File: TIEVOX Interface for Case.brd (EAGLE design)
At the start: 92.5 x 80 mm, 22 parts, among them U4 CAT24C32.UDFN8

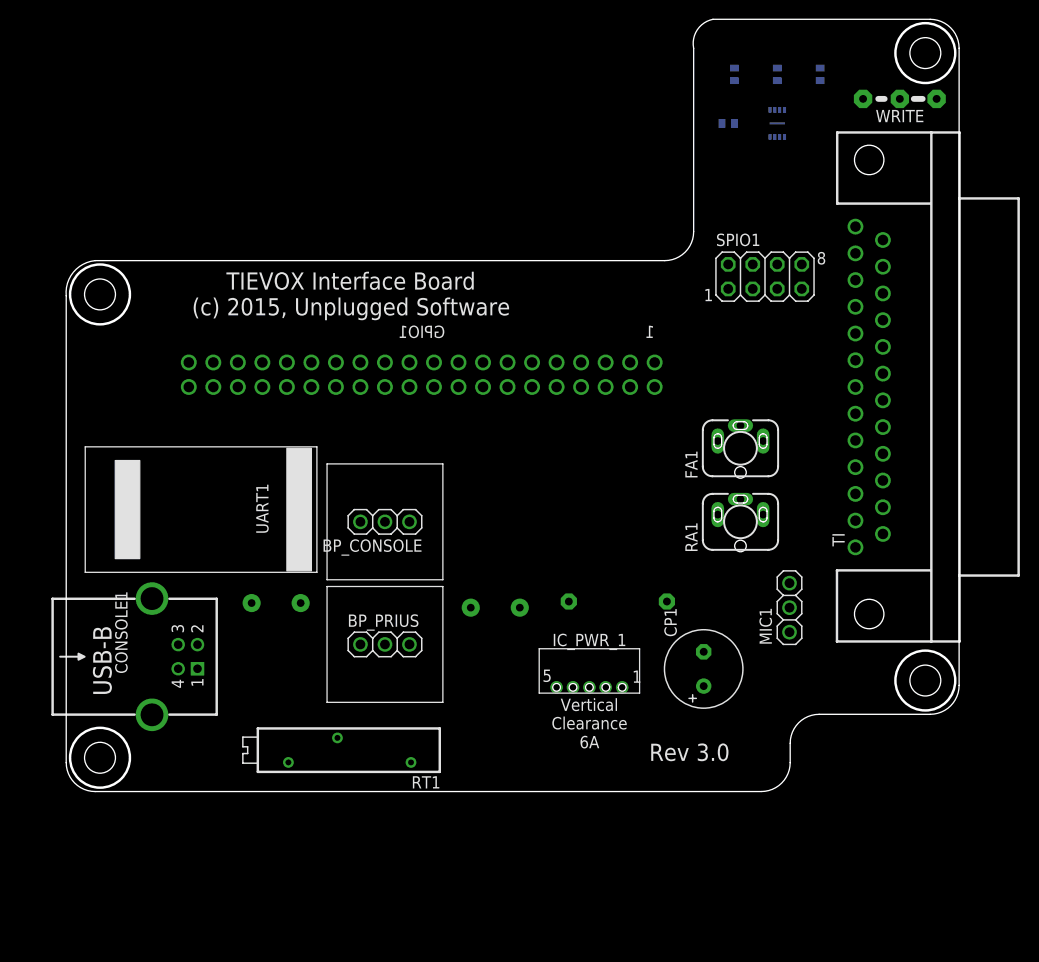
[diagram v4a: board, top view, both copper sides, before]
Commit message: Another attempt to build Interface without vias.
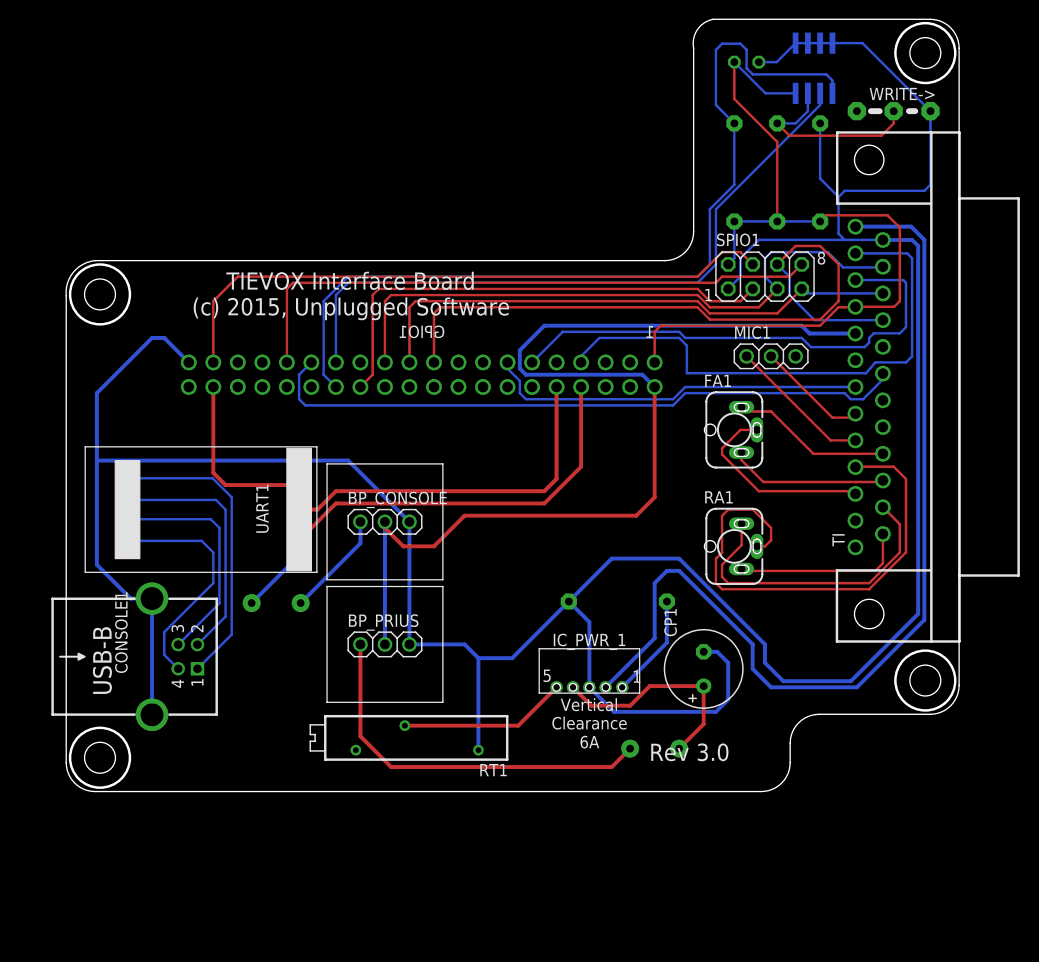
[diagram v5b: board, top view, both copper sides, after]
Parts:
- removed WRITE: (no value), jumper:04C
- added WRITE->: (no value), jumper:04C
- C1: device adafruit:C1005 -> adafruit:C025-050X050
- R6, R7, R8: device adafruit:R1005 -> adafruit:0207/10
- U4: device on-semiconductor:UDFN8 -> microbuilder:SOIC8_150MIL
- moved MIC1 26.1 mm to (73.0, 45.1), turned to 0 degrees
- moved F1 22.0 mm to (61.0, 4.45), turned to 0 degrees
- moved R6 10.2 mm to (73.7, 64.1), turned to 270 degrees
- moved R7 10.2 mm to (69.2, 64.1), turned to 270 degrees
- moved R8 10.2 mm to (78.1, 64.1), turned to 270 degrees
- moved RT1 7.10 mm to (35.1, 5.56)
- moved U4 6.87 mm to (77.5, 74.9)
- moved C1 6.63 mm to (70.5, 75.6), turned to 0 degrees
- moved RA1 2.62 mm to (69.2, 25.4), turned to 270 degrees
- moved FA1 2.01 mm to (69.2, 37.5), turned to 270 degrees
- turned BP_CONSOLE to 0 degrees
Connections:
- removed net 39_GND: GPIO1.39_GND
- new net 14_GND: GPIO1.14_GND
- new net 6_GND: GPIO1.6_GND
- net GND: now also GPIO1.39_GND, WRITE->.3; no longer GPIO1.14_GND, GPIO1.6_GND, U4.PAD, WRITE.3
- net N$39: now also WRITE->.2; no longer WRITE.2
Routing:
- net GND: track 0.00 -> 320.1 mm
- net +5VDC: track 0.00 -> 108.4 mm
- net PWR12_IN: track 0.00 -> 97.8 mm
- net N$40: track 0.00 -> 91.4 mm
- net +3.3VDC: track 0.00 -> 86.2 mm
- net N$1: track 0.00 -> 74.8 mm
- net N$38: track 0.00 -> 69.9 mm
- net N$11: track 0.00 -> 67.3 mm
- net N$3: track 0.00 -> 65.4 mm
- net N$6: track 0.00 -> 64.9 mm
- net N$5: track 0.00 -> 62.0 mm
- net N$2: track 0.00 -> 56.8 mm
- net N$7: track 0.00 -> 55.9 mm
- net N$8: track 0.00 -> 51.8 mm
- net N$21: track 0.00 -> 51.3 mm
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
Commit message: Updated TIEVOX Interface for Case:
- Removed console circuit
- Replaced audio jacks to use ones purchased
- Remapped circuit schematic
- Added backpower protection back in
- Still needs traces drawn.
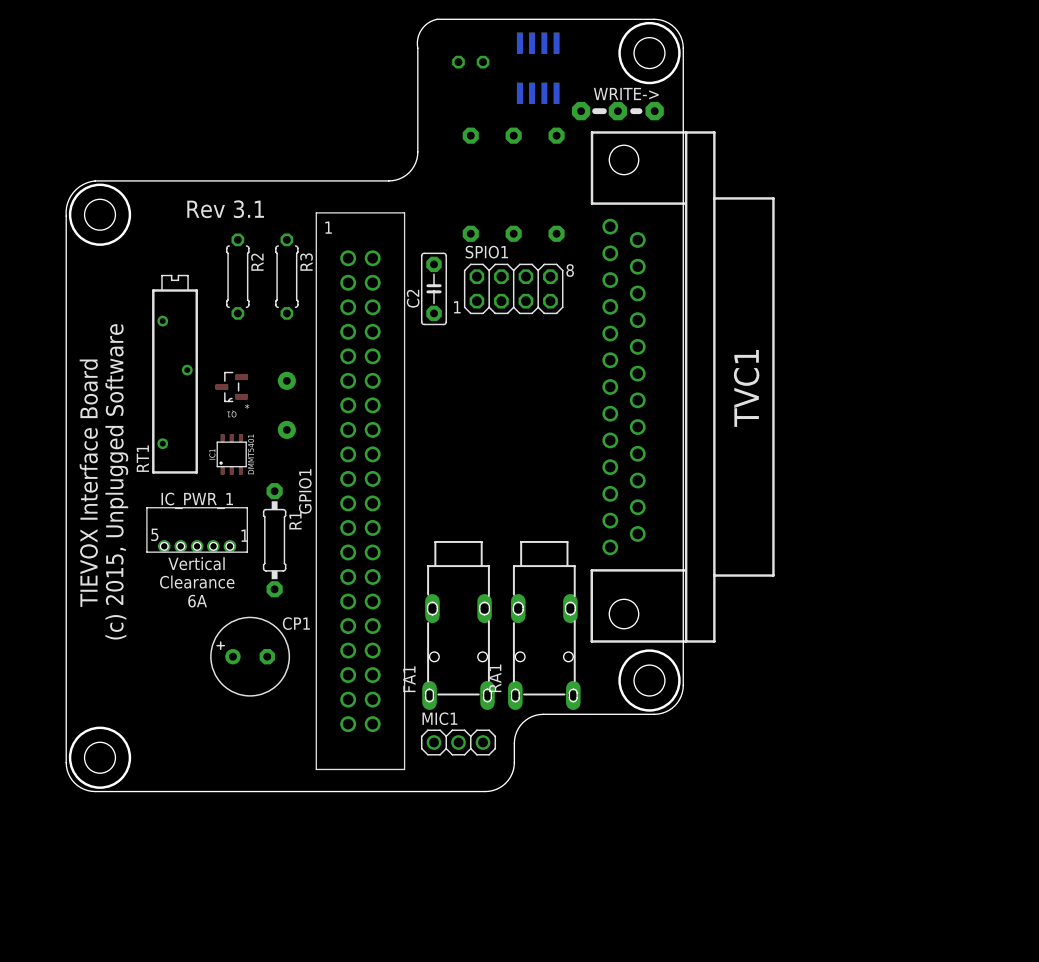
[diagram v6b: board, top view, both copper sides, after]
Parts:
- removed BP_CONSOLE, BP_PRIUS: BACKPOWER, connectors:BACKPOWER
- removed CONSOLE1: (no value), connector:USBBF-1
- removed F2: 06R155BPR, SparkFun-PowerIC:PTC
- removed TI: D-SUB25-H5R25RA, con-thomas-betts:H5R25RA
- removed UART1: GS27159, packages:GS27159
- added C2: 0.1uf, capacitor-wima:C5B2.5
- added IC1: DMMT5401, Diodes_Inc_By_element14_Batch_1:DMMT5401
- added Q1: DMP2305U-7, Diodes_Inc_By_element14_Batch_1:SOT103P240X110-3N
- added R2: 10K, 1%, adafruit:0207/7
- added R3: 47K, 1%, adafruit:0207/7
- added TVC1: TIEVox Car Interface, connectors:D-SUB25
- FA1, RA1: value 1502_01 -> 1503_07; device con-lumberg:1502_01 -> con-lumberg:1503_07
- GPIO1: value RPI_GPIO_FEMALE_LOWER -> RPI_GPIO_MALE_SHROUD; device connectors:RPI_GPIO_FEMALE_BOTTOM -> connectors:RPI_GPIO_MALE
- moved F1 52.1 mm to (22.9, 40.0), turned to 90 degrees
- moved MIC1 51.5 mm to (40.6, 5.08)
- moved CP1 47.0 mm to (19.1, 14.0), turned to 0 degrees
- moved RT1 44.9 mm to (11.3, 43.7), turned to 90 degrees
- moved IC_PWR_1 43.2 mm to (10.2, 25.4)
- moved R1 36.1 mm to (21.6, 26.0), flipped to the top, turned to 270 degrees
- moved FA1 33.0 mm to (40.6, 21.0), turned to 0 degrees
- moved C1 28.6 mm to (41.9, 75.6)
- moved U4 28.6 mm to (48.9, 74.9)
- moved WRITE-> 28.6 mm to (55.2, 70.5)
- moved R7 27.3 mm to (41.9, 62.9)
- moved R8 27.3 mm to (50.8, 62.9)
- moved R6 27.3 mm to (46.4, 62.9)
- moved SPIO1 26.1 mm to (46.4, 52.1)
- moved RA1 20.2 mm to (49.5, 21.0), turned to 0 degrees
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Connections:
- removed net 14_GND: GPIO1.14_GND
- removed net 17_3.3VDC: GPIO1.17_3.3VDC
- removed net 20_GND: GPIO1.20_GND
- removed net 25_GND: GPIO1.25_GND
- removed net 30_GND: GPIO1.30_GND
- removed net 4_5VDC: GPIO1.4_5VDC
- removed net 5VDC: F2.P$1, UART1.5VDC
- removed net 6_GND: GPIO1.6_GND
- removed net 9_GND: GPIO1.9_GND
- removed net CONSOLE_ON: GPIO1.38_GPIO20, UART1.3.3VDC
- removed net N$11 (its old number): GPIO1.29_GPIO5, TI.19
- removed net N$31: BP_CONSOLE.PWR_IN, F2.P$2
- removed net N$36: MIC1.1, TI.9
- removed net N$37: MIC1.2, TI.8
- removed net N$38: GPIO1.27_ID_SD_EEPROM, U4.6
- removed net N$40: GPIO1.28_ID_SC_EEPROM, R7.1, U4.5
- removed net N$41: GPIO1.33_GPIO13, MIC1.3
- new net IN: F1.P$2, IC1.E1, Q1.3
- new net N$32: IC1.B1, IC1.B2, IC1.C1, R2.2
- new net N$33: IC1.C2, Q1.1, R3.2
- new net N$5: FA1.1, TVC1.FRONT_COMMON
- net +3.3VDC: now also C2.2, GPIO1.17_3.3VDC, TVC1.+3.3VDC_OUT; no longer TI.4
- net +5VDC: now also GPIO1.4_5VDC, IC1.E2, Q1.2, TVC1.+5VDC_OUT; no longer BP_CONSOLE.PWR_OUT, BP_PRIUS.PWR_OUT, TI.5
- net GND: now also C2.1, GPIO1.14_GND, GPIO1.20_GND, GPIO1.25_GND, GPIO1.30_GND, GPIO1.6_GND, GPIO1.9_GND, R2.1, R3.1, TVC1.GND; no longer BP_CONSOLE.GND, BP_PRIUS.GND, CONSOLE1.CASE1, CONSOLE1.CASE2, R8.1, TI.14, U4.2, U4.3, UART1.GND
- net N$1: now also U4.2, U4.3; no longer GPIO1.19_SPI0_MOSI, SPIO1.6, TI.17
- net N$10: now also GPIO1.19_SPI0_MOSI, SPIO1.6, TVC1.SPI0_MOSI; no longer GPIO1.24_SPI0_CE0, TI.18
- net N$12: now also RA1.2@1, TVC1.SOUND_RR; no longer GPIO1.16_GPIO23, TI.20
- net N$13: now also RA1.3, TVC1.SOUND_RL; no longer GPIO1.15_GPIO22, TI.21
- net N$14: now also FA1.2@1, TVC1.SOUND_FR; no longer CONSOLE1.4, UART1.USB_GND
- net N$15: now also FA1.3, TVC1.SOUND_FL; no longer CONSOLE1.1, UART1.USB_5VDC
- net N$16: now also MIC1.1, TVC1.MIC_IN; no longer CONSOLE1.2, UART1.USB_D-
- net N$17: now also MIC1.2, TVC1.MIC_COMMON; no longer CONSOLE1.3, UART1.USB_D+
- net N$18: now also GPIO1.5_I2C1_SCL, TVC1.I2C1_SCL; no longer GPIO1.8_UART_TXD, UART1.TXD
- net N$19: now also GPIO1.3_I2C1_SDA, TVC1.I2C1_SDA; no longer GPIO1.10_UART_RXD, UART1.RXD
- net N$2: now also GPIO1.28_ID_SC_EEPROM, R7.1, U4.6; no longer GPIO1.21_SPI0_MISO, SPIO1.7, TI.16
- net N$20: now also GPIO1.24_SPI0_CE0, TVC1.SPI0_CE0; no longer FA1.1, TI.11
- net N$21: now also GPIO1.37_GPIO26, TVC1.ACCESSORY; no longer RA1.1, TI.10
- net N$22: now also GPIO1.35_GPIO19, MIC1.3; no longer RA1.2, TI.24
- net N$23: now also GPIO1.13_GPIO27, TVC1.AMP_ENABLE; no longer RA1.3, TI.25
- net N$24: now also GPIO1.7_GPIO4, TVC1.ON_SWITCH; no longer FA1.3, TI.23
- net N$25: now also GPIO1.38_GPIO20, TVC1.ON_LAMP; no longer FA1.2, TI.22
- net N$26: now also GPIO1.29_GPIO5, TVC1.SW_FLOOR_PEDAL; no longer GPIO1.3_I2C1_SDA, TI.12
- net N$27: now also GPIO1.15_GPIO22, TVC1.SW_RIGHT_TRIGGER; no longer GPIO1.5_I2C1_SCL, TI.13
- net N$3: now also GPIO1.27_ID_SD_EEPROM, R8.1, U4.5; no longer GPIO1.23_SPI0_SCLK, SPIO1.5, TI.15
- net N$30: now also GPIO1.16_GPIO23, TVC1.SW_LEFT_TRIGGER; no longer BP_PRIUS.PWR_IN, F1.P$2
- net N$4: now also GPIO1.22_GPIO25; no longer GPIO1.26_SPI0_CE1
- net N$6: now also RA1.1, TVC1.REAR_COMMON; no longer GPIO1.37_GPIO26, SPIO1.4
- net N$7: now also GPIO1.26_SPI0_CE1, SPIO1.4; no longer GPIO1.7_GPIO4, TI.2
- net N$8: now also GPIO1.23_SPI0_SCLK, SPIO1.5, TVC1.SPI0_SCLK; no longer GPIO1.11_GPIO17, TI.3
- net N$9: now also GPIO1.21_SPI0_MISO, SPIO1.7, TVC1.SPI0_MISO; no longer GPIO1.13_GPIO27, TI.7
- net PWR12_IN: now also TVC1.+12VDC_IN; no longer TI.1
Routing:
- net GND: track 320.1 -> 0.00 mm
- net +5VDC: track 108.4 -> 0.00 mm
- net PWR12_IN: track 97.8 -> 0.00 mm
- net N$40: track 91.4 -> 0.00 mm
- net +3.3VDC: track 86.2 -> 0.00 mm
- net N$1: track 74.8 -> 0.00 mm
- net N$38: track 69.9 -> 0.00 mm
- net N$11 (its old number): track 67.3 -> 0.00 mm
- net N$3: track 65.4 -> 0.00 mm
- net N$6: track 64.9 -> 0.00 mm
- net N$11: track 62.0 -> 0.00 mm
- net N$2: track 56.8 -> 0.00 mm
- net N$7: track 55.9 -> 0.00 mm
- net N$8: track 51.8 -> 0.00 mm
- net N$21: track 51.3 -> 0.00 mm
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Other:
- board size 92.5 x 80 mm -> 63.9 x 80 mm
- board text added: "Rev 3.1"
- board text removed: "Rev 3.0"

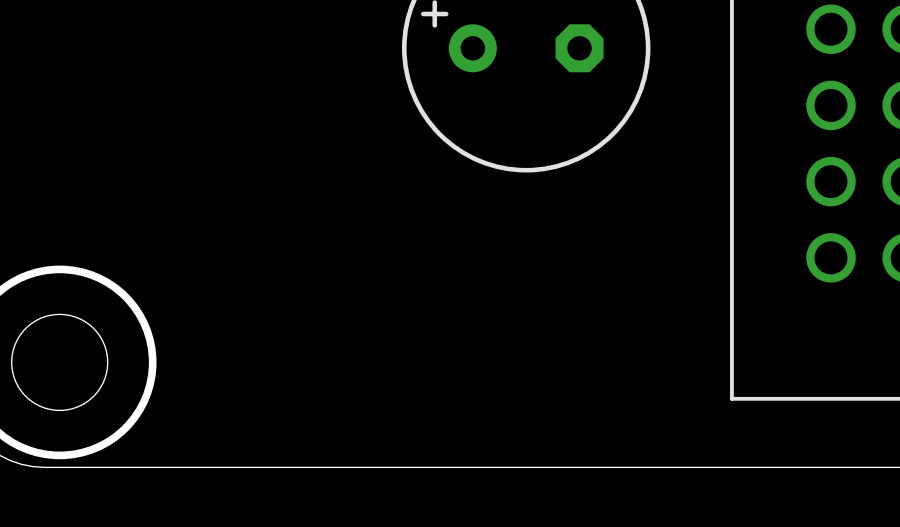
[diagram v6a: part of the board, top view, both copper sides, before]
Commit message: Added printables for split/protect circuit for fab of board.
Added Accessory Relay header to interface board.
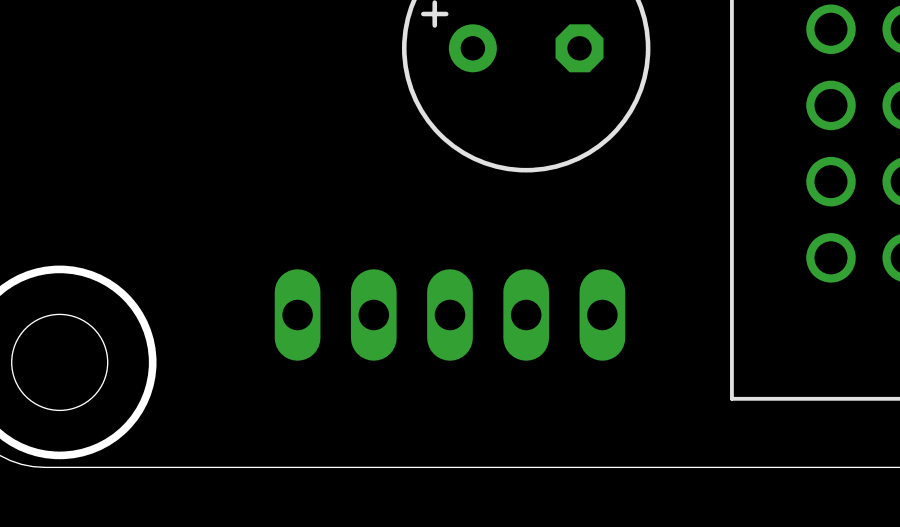
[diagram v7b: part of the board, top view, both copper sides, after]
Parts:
- added RL1: (no value), con-lstb:MA05-1
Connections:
- new net N$31: RL1.3
- net +3.3VDC: now also RL1.5
- net GND: now also RL1.1
- net N$21: now also RL1.2; no longer GPIO1.37_GPIO26
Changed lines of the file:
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@@
 <element name="TVC1" library="connectors" package="D-SUB25" value="TIEVox Car Interface" x="57.785" y="41.91" rot="R90"/>
 <element name="C2" library="capacitor-wima" package="C5B2.5" value="0.1uf" x="38.1" y="52.07" rot="R90"/>
+<element name="RL1" library="con-lstb" package="MA05-1" value="" x="16.51" y="5.08" rot="MR0">
+<attribute name="OC_NEWARK" value="unknown" x="16.51" y="5.08" size="1.778" layer="28" rot="MR0" display="off"/>
+<attribute name="MPN" value="" x="16.51" y="5.08" size="1.778" layer="28" rot="MR0" display="off"/>
+<attribute name="OC_FARNELL" value="unknown" x="16.51" y="5.08" size="1.778" layer="28" rot="MR0" display="off"/>
+<attribute name="MF" value="" x="16.51" y="5.08" size="1.778" layer="28" rot="MR0" display="off"/>
+</element>
 </elements>
 <signals>
@@
 <contactref element="C2" pad="1"/>
 <contactref element="TVC1" pad="GND"/>
+<contactref element="RL1" pad="1"/>
 <wire x1="50.8" y1="77.53" x2="60.96" y2="70.485" width="0" layer="19" extent="16-16"/>
 <wire x1="46.99" y1="77.53" x2="50.8" y2="77.53" width="0" layer="19" extent="16-16"/>
@@
 <wire x1="42.545" y1="50.8" x2="59.2074" y2="57.1373" width="0" layer="19" extent="1-1"/>
 <wire x1="38.1" y1="49.53" x2="42.545" y2="50.8" width="0" layer="19" extent="1-1"/>
-<wire x1="31.75" y1="50.165" x2="42.545" y2="50.8" width="0" layer="19" extent="1-1"/>
+<wire x1="31.75" y1="50.165" x2="38.1" y2="49.53" width="0" layer="19" extent="1-1"/>
 <wire x1="29.21" y1="45.085" x2="31.75" y2="50.165" width="0" layer="19" extent="1-1"/>
 <wire x1="31.75" y1="40.005" x2="29.21" y2="45.085" width="0" layer="19" extent="1-1"/>
@@
 <wire x1="22.86" y1="57.15" x2="31.75" y2="50.165" width="0" layer="19" extent="1-1"/>
 <wire x1="17.78" y1="57.15" x2="22.86" y2="57.15" width="0" layer="19" extent="1-1"/>
-<wire x1="20.828" y1="13.97" x2="13.56" y2="25.4" width="0" layer="19" extent="1-1"/>
+<wire x1="20.828" y1="13.97" x2="31.75" y2="19.685" width="0" layer="19" extent="1-1"/>
 <wire x1="29.21" y1="6.985" x2="20.828" y2="13.97" width="0" layer="19" extent="1-1"/>
+<wire x1="21.59" y1="5.08" x2="20.828" y2="13.97" width="0" layer="19" extent="1-1"/>
 </signal>
 <signal name="+3.3VDC">
@@
 <contactref element="C2" pad="2"/>
 <contactref element="TVC1" pad="+3.3VDC_OUT"/>
+<contactref element="RL1" pad="5"/>
 <wire x1="40.64" y1="75.565" x2="46.99" y2="72.33" width="0" layer="19" extent="16-16"/>
 <wire x1="46.355" y1="57.785" x2="46.99" y2="72.33" width="0" layer="19" extent="16-16"/>
@@
 <wire x1="41.91" y1="57.785" x2="46.355" y2="57.785" width="0" layer="19" extent="1-1"/>
 <wire x1="42.545" y1="53.34" x2="41.91" y2="57.785" width="0" layer="19" extent="1-1"/>
+<wire x1="38.1" y1="54.61" x2="42.545" y2="53.34" width="0" layer="19" extent="1-1"/>
+<wire x1="29.21" y1="55.245" x2="38.1" y2="54.61" width="0" layer="19" extent="1-1"/>
 <wire x1="56.3626" y1="50.2158" x2="50.8" y2="57.785" width="0" layer="19" extent="1-1"/>
-<wire x1="38.1" y1="54.61" x2="42.545" y2="53.34" width="0" layer="19" extent="1-1"/>
-<wire x1="29.21" y1="55.245" x2="41.91" y2="57.785" width="0" layer="19" extent="1-1"/>
-<wire x1="29.21" y1="34.925" x2="38.1" y2="54.61" width="0" layer="19" extent="1-1"/>
+<wire x1="29.21" y1="34.925" x2="29.21" y2="55.245" width="0" layer="19" extent="1-1"/>
+<wire x1="11.43" y1="5.08" x2="29.21" y2="34.925" width="0" layer="19" extent="1-1"/>
 </signal>
 <signal name="PWR12_TRIM">
@@
 <wire x1="31.75" y1="27.305" x2="59.2074" y2="46.0629" width="0" layer="19" extent="1-1"/>
 </signal>
-<signal name="N$21">
-<contactref element="TVC1" pad="ACCESSORY"/>
-<contactref element="GPIO1" pad="37_GPIO26"/>
-<wire x1="29.21" y1="9.525" x2="56.3626" y2="44.6786" width="0" layer="19" extent="1-1"/>
-</signal>
 <signal name="N$22">
 <contactref element="GPIO1" pad="35_GPIO19"/>
@@
 <wire x1="31.75" y1="37.465" x2="59.2074" y2="40.5257" width="0" layer="19" extent="1-1"/>
 </signal>
+<signal name="N$21">
+<contactref element="TVC1" pad="ACCESSORY"/>
+<contactref element="RL1" pad="2"/>
+<wire x1="19.05" y1="5.08" x2="56.3626" y2="44.6786" width="0" layer="19" extent="1-1"/>
+</signal>
+<signal name="N$31">
+<contactref element="RL1" pad="3"/>
+</signal>
 </signals>
